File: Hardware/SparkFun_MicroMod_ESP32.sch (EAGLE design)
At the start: 47 parts, among them J1 MICROMOD-2222, Q2 MBT3904DW1T1, U1 W25QXX128MBIT-6X5, U2 ESP32, U4 CP2102N, Y1 40MHz, Y2 32.768kHz

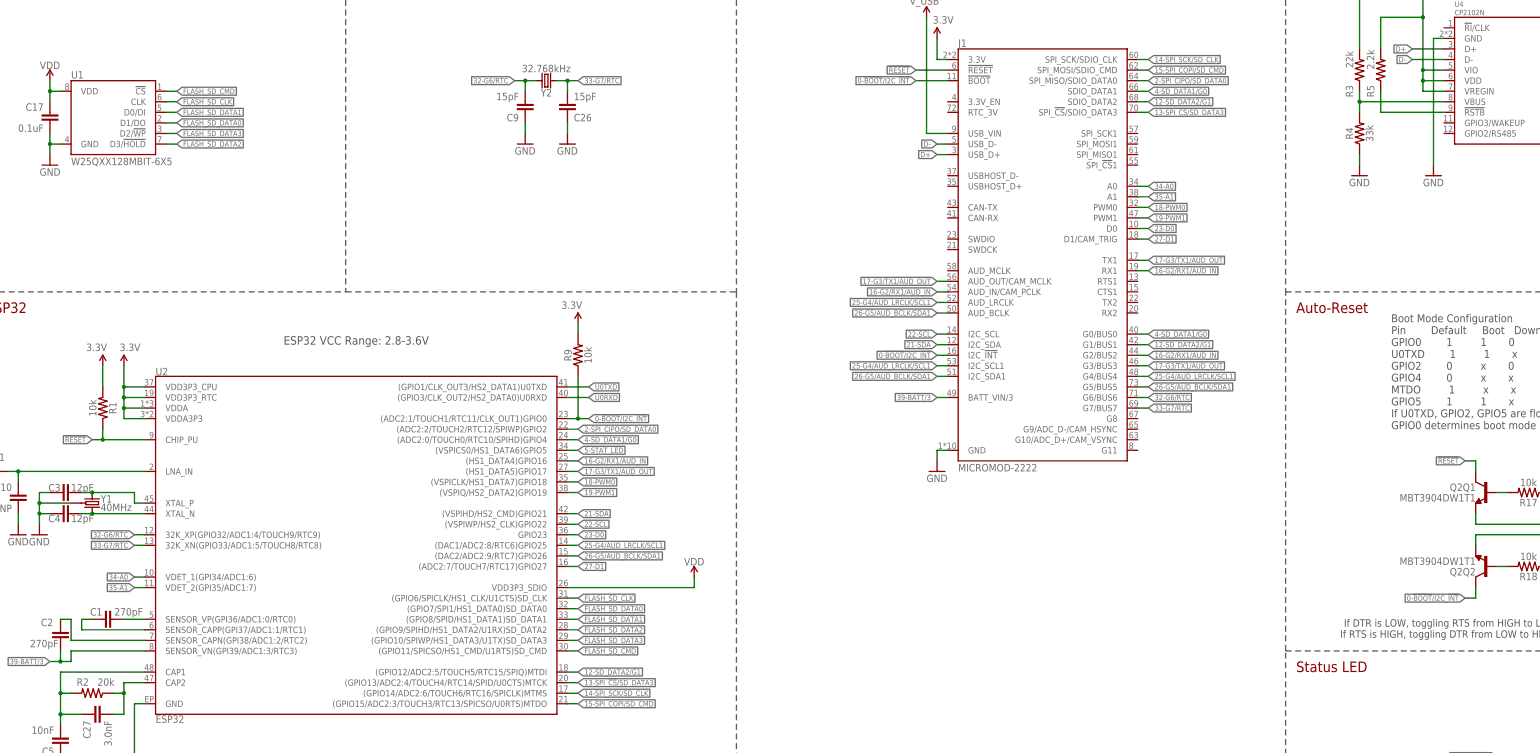
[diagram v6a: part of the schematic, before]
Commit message: v10 fix
Rearranged GPIO pins

-Boot was removed from I2C_INT
-GPIO4 was moved from G0 to I2C_INT
-GPIO12 was moved from G1 to G4
-Moved GPIO25/26 from G4/5 to G0/1
-Swapped GPIO16/17 from G2/3 to G3/2
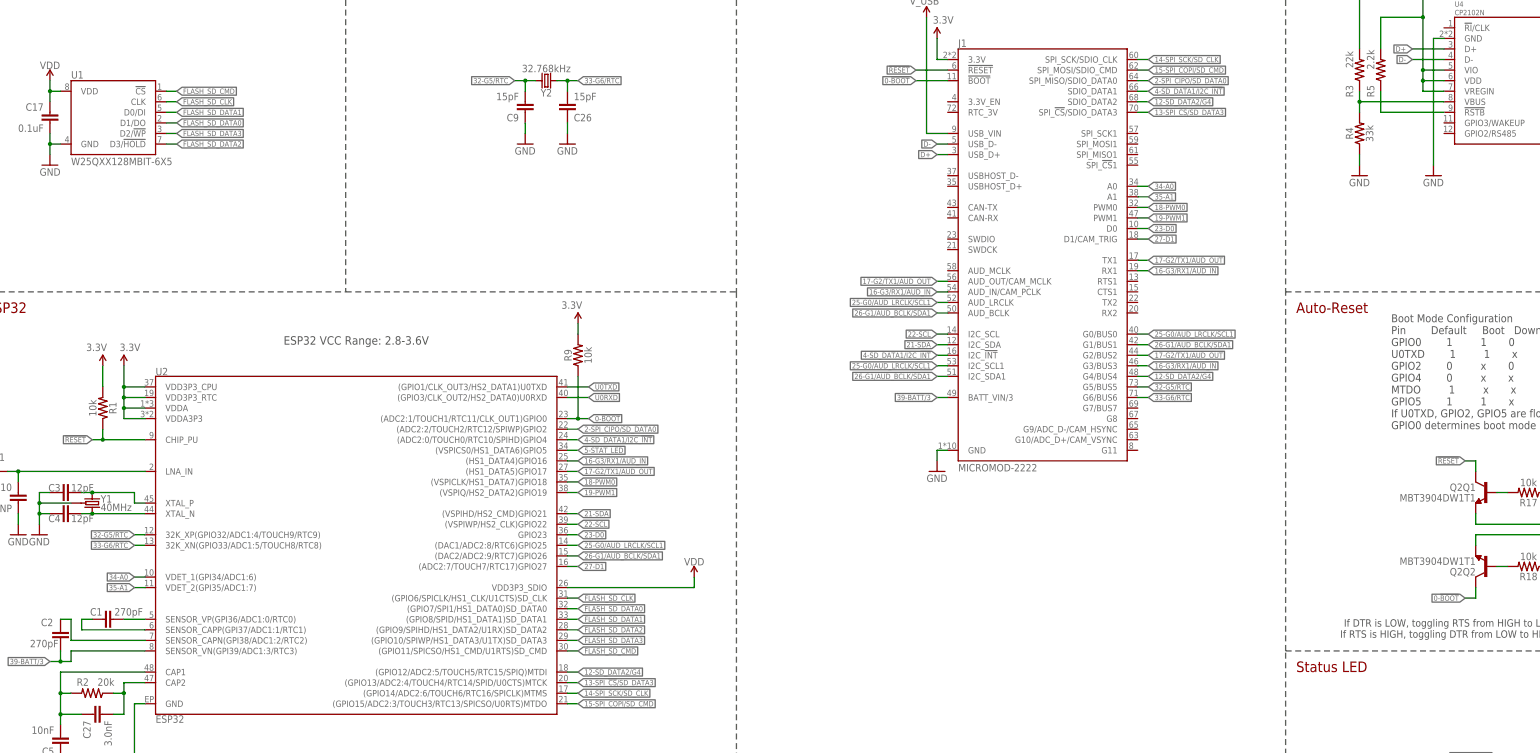
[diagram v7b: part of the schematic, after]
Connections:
- removed net 0-!BOOT!/I2C_!INT: J1.!BOOT!, J1.I2C_!INT!, Q2Q2.C, R9.1, U2.(ADC2:1/TOUCH1/RTC11/CLK_OUT1)GPIO0
- removed net 12-SD_DATA2/G1: J1.G1/BUS1, J1.SDIO_DATA2, U2.(GPIO12/ADC2:5/TOUCH5/RTC15/SPIQ)MTDI
- removed net 16-G2/RX1/AUD_IN: J1.AUD_IN/CAM_PCLK, J1.G2/BUS2, J1.RX1, U2.(HS1_DATA4)GPIO16
- removed net 17-G3/TX1/AUD_OUT: J1.AUD_OUT/CAM_MCLK, J1.G3/BUS3, J1.TX1, U2.(HS1_DATA5)GPIO17
- removed net 25-G4/AUD_LRCLK/SCL1: J1.AUD_LRCLK, J1.G4/BUS4, J1.I2C_SCL1, U2.(DAC1/ADC2:8/RTC6)GPIO25
- removed net 26-G5/AUD_BCLK/SDA1: J1.AUD_BCLK, J1.G5/BUS5, J1.I2C_SDA1, U2.(DAC2/ADC2:9/RTC7)GPIO26
- removed net 32-G6/RTC: C9.2, J1.G6/BUS6, U2.32K_XP(GPIO32/ADC1:4/TOUCH9/RTC9), Y2.1
- removed net 33-G7/RTC: C26.2, J1.G7/BUS7, U2.32K_XN(GPIO33/ADC1:5/TOUCH8/RTC8), Y2.2
- removed net 4-SD_DATA1/G0: J1.G0/BUS0, J1.SDIO_DATA1, U2.(ADC2:0/TOUCH0/RTC10/SPIHD)GPIO4
- new net 0-!BOOT!: J1.!BOOT!, Q2Q2.C, R9.1, U2.(ADC2:1/TOUCH1/RTC11/CLK_OUT1)GPIO0
- new net 12-SD_DATA2/G4: J1.G4/BUS4, J1.SDIO_DATA2, U2.(GPIO12/ADC2:5/TOUCH5/RTC15/SPIQ)MTDI
- new net 16-G3/RX1/AUD_IN: J1.AUD_IN/CAM_PCLK, J1.G3/BUS3, J1.RX1, U2.(HS1_DATA4)GPIO16
- new net 17-G2/TX1/AUD_OUT: J1.AUD_OUT/CAM_MCLK, J1.G2/BUS2, J1.TX1, U2.(HS1_DATA5)GPIO17
- new net 25-G0/AUD_LRCLK/SCL1: J1.AUD_LRCLK, J1.G0/BUS0, J1.I2C_SCL1, U2.(DAC1/ADC2:8/RTC6)GPIO25
- new net 26-G1/AUD_BCLK/SDA1: J1.AUD_BCLK, J1.G1/BUS1, J1.I2C_SDA1, U2.(DAC2/ADC2:9/RTC7)GPIO26
- new net 32-G5/RTC: C9.2, J1.G5/BUS5, U2.32K_XP(GPIO32/ADC1:4/TOUCH9/RTC9), Y2.1
- new net 33-G6/RTC: C26.2, J1.G6/BUS6, U2.32K_XN(GPIO33/ADC1:5/TOUCH8/RTC8), Y2.2
- new net 4-SD_DATA1/I2C_!INT: J1.I2C_!INT!, J1.SDIO_DATA1, U2.(ADC2:0/TOUCH0/RTC10/SPIHD)GPIO4

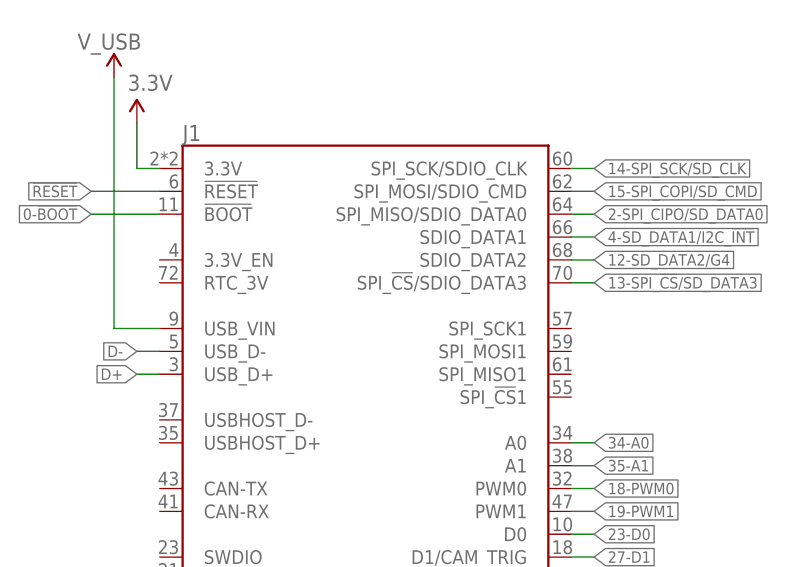
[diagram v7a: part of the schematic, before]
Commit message: Updated MicroMod Connector Schematic Symbol
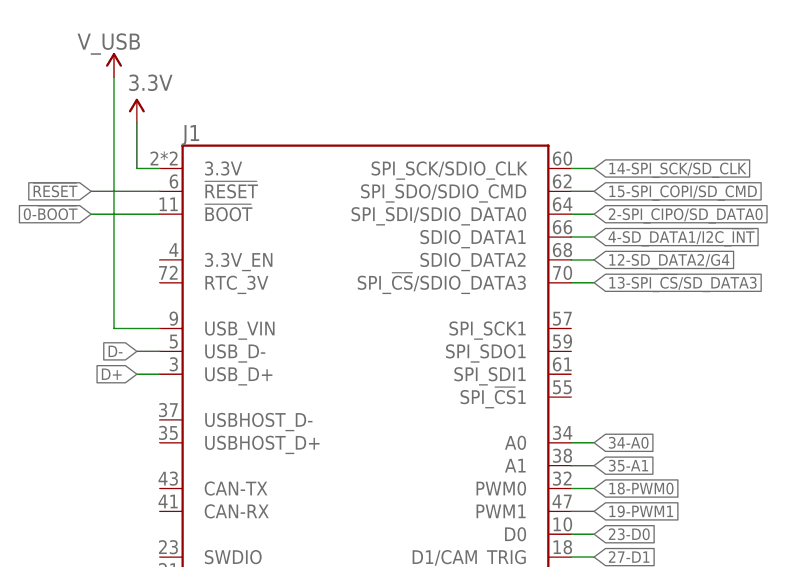
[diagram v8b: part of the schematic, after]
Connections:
- net 15-SPI_COPI/SD_CMD: now also J1.SPI_SDO/SDIO_CMD; no longer J1.SPI_MOSI/SDIO_CMD
- net 2-SPI_CIPO/SD_DATA0: now also J1.SPI_SDI/SDIO_DATA0; no longer J1.SPI_MISO/SDIO_DATA0
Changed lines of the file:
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@@
 <wire x1="294.64" y1="246.38" x2="297.18" y2="246.38" width="0.1524" layer="91"/>
 <label x="297.18" y="246.38" size="1.27" layer="95" font="vector" xref="yes"/>
-<pinref part="J1" gate="J1" pin="SPI_MOSI/SDIO_CMD"/>
+<pinref part="J1" gate="J1" pin="SPI_SDO/SDIO_CMD"/>
 </segment>
 </net>
@@
 <wire x1="294.64" y1="243.84" x2="297.18" y2="243.84" width="0.1524" layer="91"/>
 <label x="297.18" y="243.84" size="1.27" layer="95" font="vector" xref="yes"/>
-<pinref part="J1" gate="J1" pin="SPI_MISO/SDIO_DATA0"/>
-</segment>
-</net>
+<pinref part="J1" gate="J1" pin="SPI_SDI/SDIO_DATA0"/>
+</segment>
+</net>
